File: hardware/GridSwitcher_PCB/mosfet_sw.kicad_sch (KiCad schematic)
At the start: 9 parts, among them Q2 DMP3013SFV, U3 PC817, U4 PC817

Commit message: -enh made some progress on pcb/fp design
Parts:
- R107, R109, R110, R80: footprint (none) -> Resistor_SMD:R_0603_1608Metric_Pad0.98x0.95mm_HandSolder
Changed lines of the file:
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@@
       (effects (font (size 1.27 1.27)))
     )
-    (property "Footprint" "" (at 102.87 108.458 90)
+    (property "Footprint" "Resistor_SMD:R_0603_1608Metric_Pad0.98x0.95mm_HandSolder" (at 102.87 108.458 90)
       (effects (font (size 1.27 1.27)) hide)
     )
@@
       (effects (font (size 1.27 1.27)) (justify left))
     )
-    (property "Footprint" "" (at 82.042 101.6 90)
+    (property "Footprint" "Resistor_SMD:R_0603_1608Metric_Pad0.98x0.95mm_HandSolder" (at 82.042 101.6 90)
       (effects (font (size 1.27 1.27)) hide)
     )
@@
       (effects (font (size 1.27 1.27)) (justify left))
     )
-    (property "Footprint" "" (at 98.552 90.17 90)
+    (property "Footprint" "Resistor_SMD:R_0603_1608Metric_Pad0.98x0.95mm_HandSolder" (at 98.552 90.17 90)
       (effects (font (size 1.27 1.27)) hide)
     )
@@
       (effects (font (size 1.27 1.27)))
     )
-    (property "Footprint" "" (at 80.01 83.058 90)
-      (effects (font (size 1.27 1.27)) hide)
-    )
+    (property "Footprint" "Resistor_SMD:R_0603_1608Metric_Pad0.98x0.95mm_HandSolder" (at 80.01 83.058 90)
+      (effects (font (size 1.27 1.27)) hide)
+    )

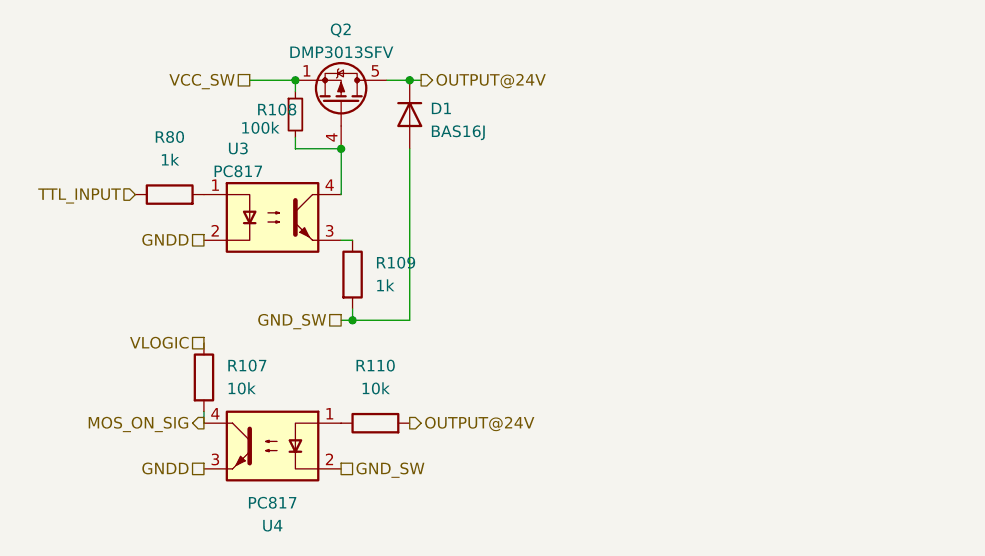
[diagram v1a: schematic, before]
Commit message: -add some changes to schematic, tested the interfaces (uart, spi and i2c) with some test code
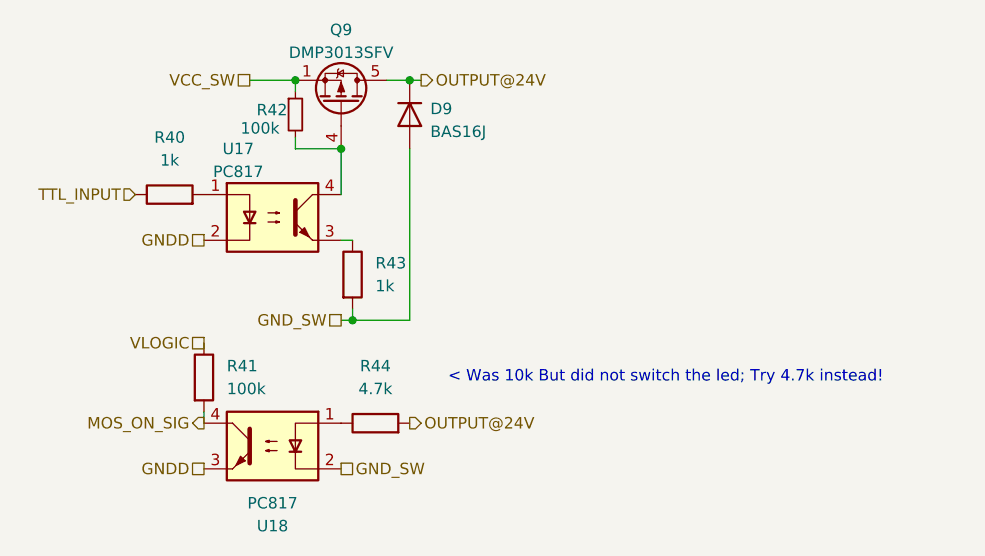
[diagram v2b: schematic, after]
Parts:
- R41: renamed from R107; value 10k -> 100k
- R44: renamed from R110; value 10k -> 4.7k
- renumbered D1 to D9, Q2 to Q9, R80 to R40, R108 to R42, R109 to R43, U3 to U17, U4 to U18
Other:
- note added: "< Was 10k But did not switch the led; Try 4.7k instead!"

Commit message: -enh final revision; ordered
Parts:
- U17, U18: footprint Package_DIP:DIP-4_W7.62mm -> Package_DIP:DIP-4_W7.62mm_SMDSocket_SmallPads
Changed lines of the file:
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@@
 			)
 		)
-		(property "Footprint" "Package_DIP:DIP-4_W7.62mm"
+		(property "Footprint" "Package_DIP:DIP-4_W7.62mm_SMDSocket_SmallPads"
 			(at 96.52 114.3 0)
 			(effects
@@
 			)
 		)
-		(property "Footprint" "Package_DIP:DIP-4_W7.62mm"
+		(property "Footprint" "Package_DIP:DIP-4_W7.62mm_SMDSocket_SmallPads"
 			(at 86.36 88.9 0)
 			(effects
